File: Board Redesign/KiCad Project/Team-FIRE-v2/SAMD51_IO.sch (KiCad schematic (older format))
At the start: 20 parts, among them U5 SAMD51, Y1 32.768kHz

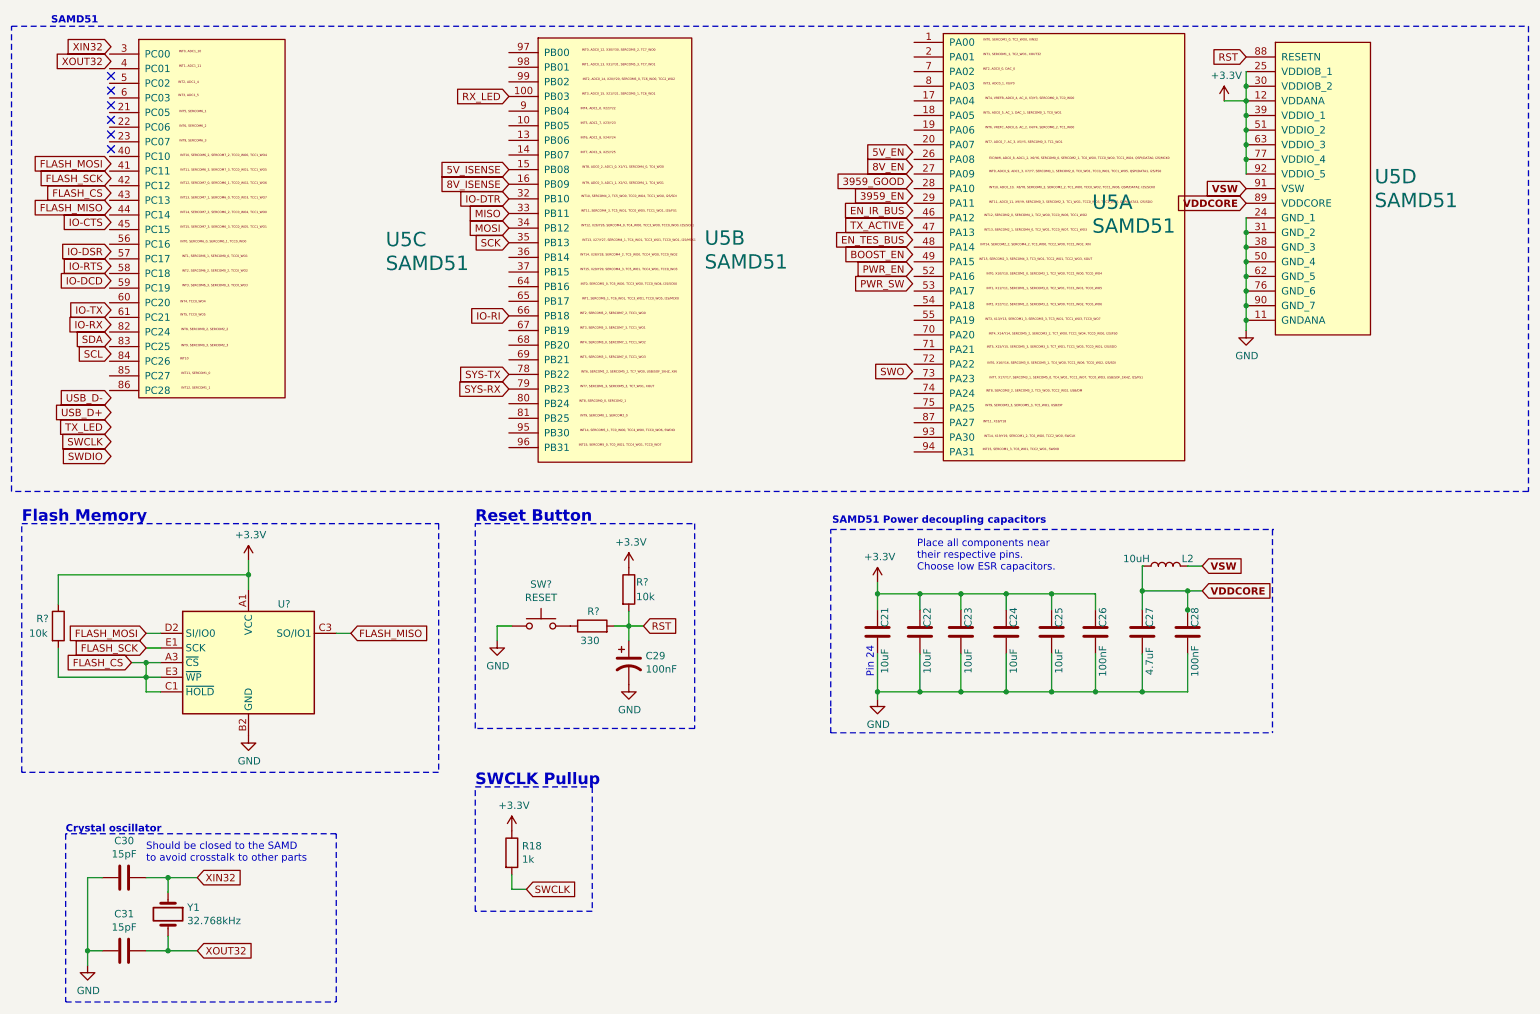
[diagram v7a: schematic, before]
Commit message: Fix positioning of SAMD51
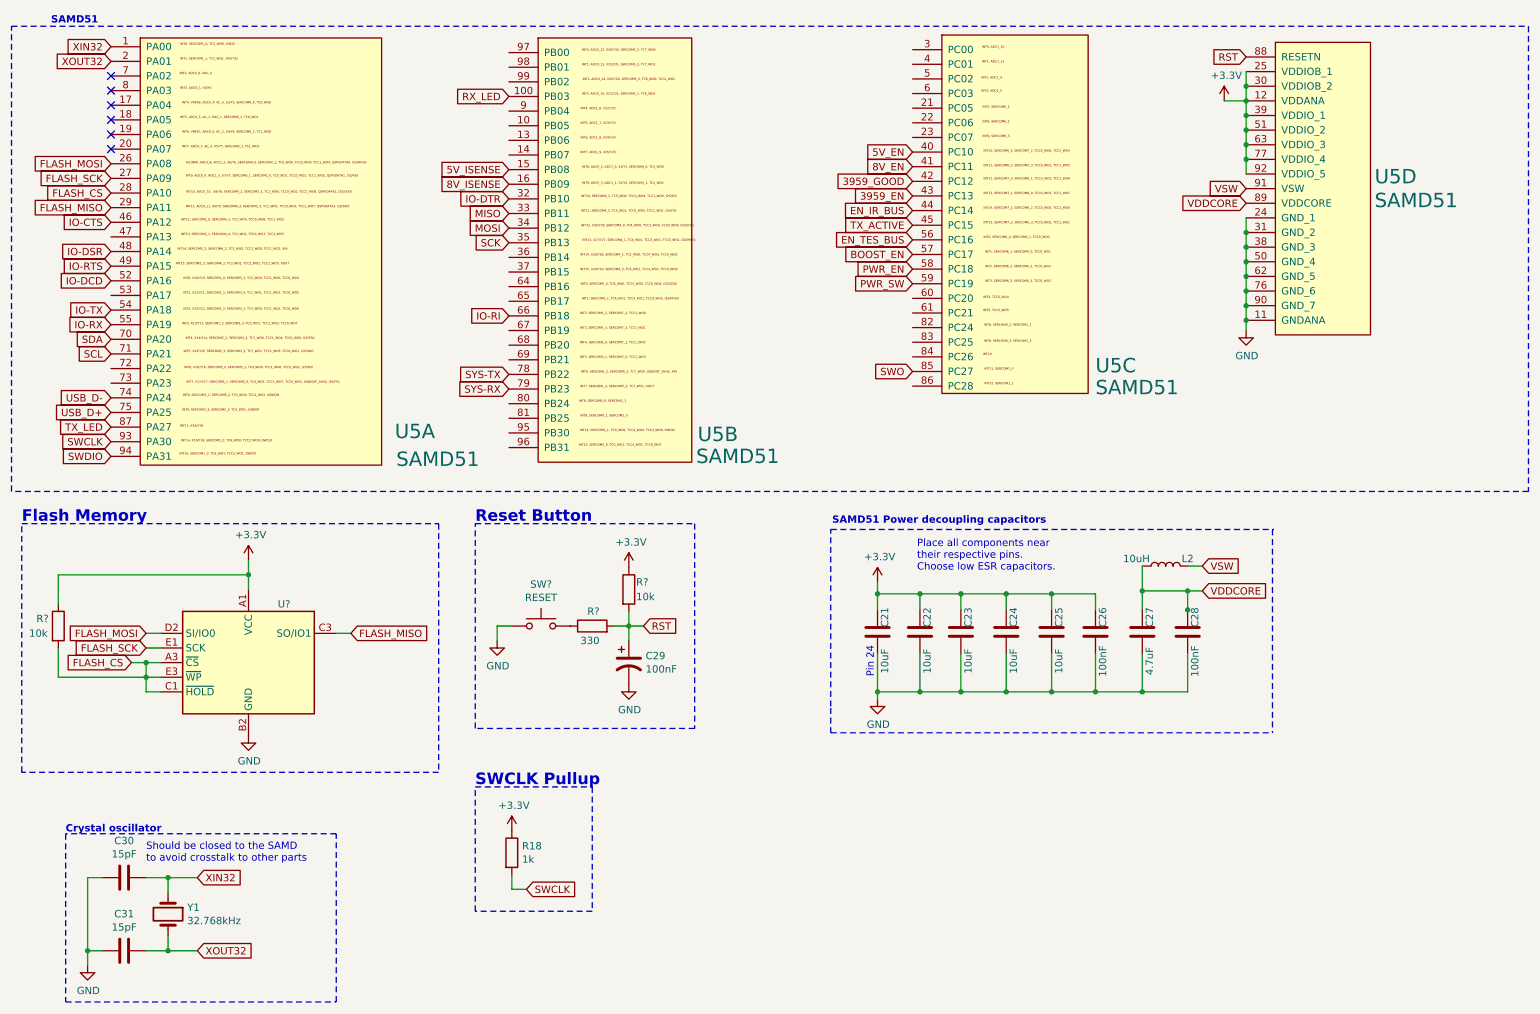
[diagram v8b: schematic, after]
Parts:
- U5: Link (none) -> https://www.digikey.com/product-detail/en/microchip-technol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; MPN ATSAMD51N20A-AU -> ATSAMD51N20A-AUT; Manufacturer (none) -> Microchip Technology; Supplier (none) -> Digikey; Supplier PN (none) -> ATSAMD51N20A-AUTCT-ND; Type (none) -> IC MCU
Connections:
- net 3959_EN: now also U5.43 (PC13)
- net 3959_GOOD: now also U5.42 (PC12)
- net 5V_EN: now also U5.40 (PC10)
- net 8V_EN: now also U5.41 (PC11)
- net BOOST_EN: now also U5.57 (PC17)
- net EN_IR_BUS: now also U5.44 (PC14)
- net EN_TES_BUS: now also U5.56 (PC16)
- net FLASH_CS: now also U5.28 (PA10)
- net FLASH_MISO: now also U5.29 (PA11)
- net FLASH_MOSI: now also U5.26 (PA08)
- net FLASH_SCK: now also U5.27 (PA09)
- net IO-CTS: now also U5.46 (PA12)
- net IO-DCD: now also U5.52 (PA16)
- net IO-DSR: now also U5.48 (PA14)
- net IO-RTS: now also U5.49 (PA15)
- net IO-RX: now also U5.55 (PA19)
- net IO-TX: now also U5.54 (PA18)
- net PWR_EN: now also U5.58 (PC18)
- net PWR_SW: now also U5.59 (PC19)
- net SCL: now also U5.71 (PA21)
- net SDA: now also U5.70 (PA20)
- net SWCLK: now also U5.93 (PA30)
- net SWDIO: now also U5.94 (PA31)
- net SWO: now also U5.85 (PC27)
- net TX_ACTIVE: now also U5.45 (PC15)
- net TX_LED: now also U5.87 (PA27)
- net USB_D+: now also U5.75 (PA25)
- net USB_D-: now also U5.74 (PA24)
- net XIN32: now also U5.1 (PA00)
- net XOUT32: now also U5.2 (PA01)
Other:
- moved on the sheet: U5A, U5C
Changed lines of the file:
@@
 EESchema Schematic File Version 4
-LIBS:Team-FIRE-v2-cache
 EELAYER 30 0
 EELAYER END
@@
 AR Path="/5E4F8378/5ED61C09" Ref="U?"  Part="2"
 AR Path="/5E4F8378/5ED4DEFC/5ED61C09" Ref="U5"  Part="2"
-F 0 "U5" H 5318 2362 98  0000 L CNN
-F 1 "SAMD51" H 5318 2199 98  0000 L CNN
+F 0 "U5" H 5270 1020 98  0000 L CNN
+F 1 "SAMD51" H 5260 870 98  0000 L CNN
 F 2 "Package_QFP:TQFP-100_14x14mm_P0.5mm" H 3930 80  28  0001 C CNN
 F 3 "http://ww1.microchip.com/downloads/en/DeviceDoc/60001507E.pdf" V 4590 1960 28  0001 C CNN
 F 4 "1.2" H 3980 180 28  0001 C CNN "Height"
-F 5 "ATSAMD51N20A-AU" H 3680 180 28  0001 C CNN "MPN"
+F 5 "ATSAMD51N20A-AUT" H 3680 180 28  0001 C CNN "MPN"
+F 6 "https://www.digikey.com/product-detail/en/microchip-technology/ATSAMD51N20A-AUT/ATSAMD51N20A-AUTCT-ND/7390168" H 4780 2230 50  0001 C CNN "Link"
+F 7 "Microchip Technology" H 4780 2230 50  0001 C CNN "Manufacturer"
+F 8 "Digikey" H 4780 2230 50  0001 C CNN "Supplier"
+F 9 "ATSAMD51N20A-AUTCT-ND" H 4780 2230 50  0001 C CNN "Supplier PN"
+F 10 "IC MCU" H 4780 2230 50  0001 C CNN "Type"
 	2    4780 2230
-	1    0    0    -1
-$EndComp
-$Comp
-L Team-FIRE:SAMD51 U?
-U 1 1 5ED61C11
-P 7550 2210
-AR Path="/5E4F8378/5ED61C11" Ref="U?"  Part="3"
-AR Path="/5E4F8378/5ED4DEFC/5ED61C11" Ref="U5"  Part="1"
-F 0 "U5" H 7968 2567 98  0000 L CNN
-F 1 "SAMD51" H 7968 2404 98  0000 L CNN
-F 2 "Package_QFP:TQFP-100_14x14mm_P0.5mm" H 6700 60  28  0001 C CNN
-F 3 "http://ww1.microchip.com/downloads/en/DeviceDoc/60001507E.pdf" V 7360 1940 28  0001 C CNN
-F 4 "1.2" H 6750 160 28  0001 C CNN "Height"
-F 5 "ATSAMD51N20A-AU" H 6450 160 28  0001 C CNN "MPN"
-	1    7550 2210
 	1    0    0    -1
 $EndComp
@@
 F 3 "http://ww1.microchip.com/downloads/en/DeviceDoc/60001507E.pdf" V 9310 1970 28  0001 C CNN
 F 4 "1.2" H 8700 190 28  0001 C CNN "Height"
-F 5 "ATSAMD51N20A-AU" H 8400 190 28  0001 C CNN "MPN"
+F 5 "ATSAMD51N20A-AUT" H 8400 190 28  0001 C CNN "MPN"
+F 6 "https://www.digikey.com/product-detail/en/microchip-technology/ATSAMD51N20A-AUT/ATSAMD51N20A-AUTCT-ND/7390168" H 9500 2240 50  0001 C CNN "Link"
+F 7 "Microchip Technology" H 9500 2240 50  0001 C CNN "Manufacturer"
+F 8 "Digikey" H 9500 2240 50  0001 C CNN "Supplier"
+F 9 "ATSAMD51N20A-AUTCT-ND" H 9500 2240 50  0001 C CNN "Supplier PN"
+F 10 "IC MCU" H 9500 2240 50  0001 C CNN "Type"
 	4    9500 2240
 	1    0    0    -1
@@
 Wire Wire Line
 	9020 2560 9020 2660
-Text GLabel 8720 4510 2    50   Input ~ 10
+Text GLabel 8720 4510 2    50   Input ~ 0
 VDDCORE
 Wire Wire Line
@@
 Wire Wire Line
 	8620 4510 8720 4510
-Text GLabel 8720 4340 2    50   Input ~ 10
+Text GLabel 8720 4340 2    50   Input ~ 0
 VSW
 Wire Wire Line
@@
 Wire Wire Line
 	6790 4530 7070 4530
-Text GLabel 9020 1860 0    50   Input ~ 10
+Text GLabel 9020 1860 0    50   Input ~ 0
 VDDCORE
-Text GLabel 9020 1760 0    50   Input ~ 10
+Text GLabel 9020 1760 0    50   Input ~ 0
 VSW
 $Comp
@@
 L Team-FIRE:SAMD51 U?
 U 3 1 5ED61BFB
-P 2060 2240
+P 7550 2210
 AR Path="/5E4F8378/5ED61BFB" Ref="U?"  Part="1"
 AR Path="/5E4F8378/5ED4DEFC/5ED61BFB" Ref="U5"  Part="3"
-F 0 "U5" H 3138 2372 98  0000 L CNN
-F 1 "SAMD51" H 3138 2209 98  0000 L CNN
-F 2 "Package_QFP:TQFP-100_14x14mm_P0.5mm" H 1210 90  28  0001 C CNN
-F 3 "http://ww1.microchip.com/downloads/en/DeviceDoc/60001507E.pdf" V 1870 1970 28  0001 C CNN
-F 4 "1.2" H 1260 190 28  0001 C CNN "Height"
-F 5 "ATSAMD51N20A-AU" H 960 190 28  0001 C CNN "MPN"
-	3    2060 2240
+F 0 "U5" H 7990 1450 98  0000 L CNN
+F 1 "SAMD51" H 7990 1300 98  0000 L CNN
+F 2 "Package_QFP:TQFP-100_14x14mm_P0.5mm" H 6700 60  28  0001 C CNN
+F 3 "http://ww1.microchip.com/downloads/en/DeviceDoc/60001507E.pdf" V 7360 1940 28  0001 C CNN
+F 4 "1.2" H 6750 160 28  0001 C CNN "Height"
+F 5 "ATSAMD51N20A-AUT" H 6450 160 28  0001 C CNN "MPN"
+F 6 "https://www.digikey.com/product-detail/en/microchip-technology/ATSAMD51N20A-AUT/ATSAMD51N20A-AUTCT-ND/7390168" H 7550 2210 50  0001 C CNN "Link"
+F 7 "Microchip Technology" H 7550 2210 50  0001 C CNN "Manufacturer"
+F 8 "Digikey" H 7550 2210 50  0001 C CNN "Supplier"
+F 9 "ATSAMD51N20A-AUTCT-ND" H 7550 2210 50  0001 C CNN "Supplier PN"
+F 10 "IC MCU" H 7550 2210 50  0001 C CNN "Type"
+	3    7550 2210
 	1    0    0    -1
 $EndComp
@@
 Wire Notes Line
 	3750 6700 3750 5850
+$Comp
+L Team-FIRE:SAMD51 U?
+U 1 1 5ED61C11
+P 2060 2240
+AR Path="/5E4F8378/5ED61C11" Ref="U?"  Part="3"
+AR Path="/5E4F8378/5ED4DEFC/5ED61C11" Ref="U5"  Part="1"
+F 0 "U5" H 3200 1060 98  0000 L CNN
+F 1 "SAMD51" H 3210 870 98  0000 L CNN
+F 2 "Package_QFP:TQFP-100_14x14mm_P0.5mm" H 1210 90  28  0001 C CNN
+F 3 "http://ww1.microchip.com/downloads/en/DeviceDoc/60001507E.pdf" V 1870 1970 28  0001 C CNN
+F 4 "1.2" H 1260 190 28  0001 C CNN "Height"
+F 5 "ATSAMD51N20A-AUT" H 960 190 28  0001 C CNN "MPN"
+F 6 "https://www.digikey.com/product-detail/en/microchip-technology/ATSAMD51N20A-AUT/ATSAMD51N20A-AUTCT-ND/7390168" H 2060 2240 50  0001 C CNN "Link"
+F 7 "Microchip Technology" H 2060 2240 50  0001 C CNN "Manufacturer"
+F 8 "Digikey" H 2060 2240 50  0001 C CNN "Supplier"
+F 9 "ATSAMD51N20A-AUTCT-ND" H 2060 2240 50  0001 C CNN "Supplier PN"
+F 10 "IC MCU" H 2060 2240 50  0001 C CNN "Type"
+	1    2060 2240
+	1    0    0    -1
+$EndComp
 $EndSCHEMATC
